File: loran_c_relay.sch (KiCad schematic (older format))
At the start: 29 parts, among them IC501 PC817, IC502 PC817, IC503 PC817, IC504 PC817, P501 RELAY A, P502 RELAY B, P503 RELAY C, P504 RELAY D, Q501 BC847, Q502 BC847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

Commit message: FIXED: no more buses on hierarchical sheet ports
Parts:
- C501: value 2.2u 6.3V -> 10u 6.3V Ta
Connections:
- net labels added: RELAY1, RELAY2, RELAY3, RELAY4
- net labels removed: BREL, REL1, REL2, REL3, REL4, RELAY
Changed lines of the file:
@@
 $Descr A4 11693 8268
 encoding utf-8
-Sheet 5 7
+Sheet 4 7
 Title ""
 Date ""
@@
 $EndComp
 $Comp
-L GND #PWR078
+L GND #PWR071
 U 1 1 52DF2D2C
 P 5500 2400
-F 0 "#PWR078" H 5500 2400 30  0001 C CNN
+F 0 "#PWR071" H 5500 2400 30  0001 C CNN
 F 1 "GND" H 5500 2330 30  0001 C CNN
 F 2 "" H 5500 2400 60  0000 C CNN
@@
 $EndComp
 $Comp
-L GND #PWR079
+L GND #PWR072
 U 1 1 52DF2D32
 P 4400 2400
-F 0 "#PWR079" H 4400 2400 30  0001 C CNN
+F 0 "#PWR072" H 4400 2400 30  0001 C CNN
 F 1 "GND" H 4400 2330 30  0001 C CNN
 F 2 "" H 4400 2400 60  0000 C CNN
@@
 $EndComp
 $Comp
-L VDD #PWR080
+L VDD #PWR073
 U 1 1 52DF2D44
 P 5150 1500
-F 0 "#PWR080" H 5150 1600 30  0001 C CNN
+F 0 "#PWR073" H 5150 1600 30  0001 C CNN
 F 1 "VDD" H 5150 1610 30  0000 C CNN
 F 2 "" H 5150 1500 60  0000 C CNN
@@
 $EndComp
 $Comp
-L GND #PWR081
+L GND #PWR074
 U 1 1 52DF2D68
 P 5500 3400
-F 0 "#PWR081" H 5500 3400 30  0001 C CNN
+F 0 "#PWR074" H 5500 3400 30  0001 C CNN
 F 1 "GND" H 5500 3330 30  0001 C CNN
 F 2 "" H 5500 3400 60  0000 C CNN
@@
 $EndComp
 $Comp
-L GND #PWR082
+L GND #PWR075
 U 1 1 52DF2D6E
 P 4400 3400
-F 0 "#PWR082" H 4400 3400 30  0001 C CNN
+F 0 "#PWR075" H 4400 3400 30  0001 C CNN
 F 1 "GND" H 4400 3330 30  0001 C CNN
 F 2 "" H 4400 3400 60  0000 C CNN
@@
 $EndComp
 $Comp
-L GND #PWR083
+L GND #PWR076
 U 1 1 52DF2D9E
 P 5500 4400
-F 0 "#PWR083" H 5500 4400 30  0001 C CNN
+F 0 "#PWR076" H 5500 4400 30  0001 C CNN
 F 1 "GND" H 5500 4330 30  0001 C CNN
 F 2 "" H 5500 4400 60  0000 C CNN
@@
 $EndComp
 $Comp
-L GND #PWR084
+L GND #PWR077
 U 1 1 52DF2DA4
 P 4400 4400
-F 0 "#PWR084" H 4400 4400 30  0001 C CNN
+F 0 "#PWR077" H 4400 4400 30  0001 C CNN
 F 1 "GND" H 4400 4330 30  0001 C CNN
 F 2 "" H 4400 4400 60  0000 C CNN
@@
 $EndComp
 $Comp
-L GND #PWR085
+L GND #PWR078
 U 1 1 52DF2DD4
 P 5500 6000
-F 0 "#PWR085" H 5500 6000 30  0001 C CNN
+F 0 "#PWR078" H 5500 6000 30  0001 C CNN
 F 1 "GND" H 5500 5930 30  0001 C CNN
 F 2 "" H 5500 6000 60  0000 C CNN
@@
 $EndComp
 $Comp
-L GND #PWR086
+L GND #PWR079
 U 1 1 52DF2DDA
 P 4400 6000
-F 0 "#PWR086" H 4400 6000 30  0001 C CNN
+F 0 "#PWR079" H 4400 6000 30  0001 C CNN
 F 1 "GND" H 4400 5930 30  0001 C CNN
 F 2 "" H 4400 6000 60  0000 C CNN
@@
 P 5150 5750
 F 0 "C501" H 5200 5850 50  0000 L CNN
-F 1 "2.2u 6.3V" H 5200 5650 50  0000 L CNN
+F 1 "10u 6.3V Ta" H 5200 5650 50  0000 L CNN
 F 2 "" H 5150 5750 60  0000 C CNN
 F 3 "" H 5150 5750 60  0000 C CNN
@@
 $EndComp
 $Comp
-L GND #PWR087
+L GND #PWR080
 U 1 1 52DF2DFE
 P 5150 6000
-F 0 "#PWR087" H 5150 6000 30  0001 C CNN
+F 0 "#PWR080" H 5150 6000 30  0001 C CNN
 F 1 "GND" H 5150 5930 30  0001 C CNN
 F 2 "" H 5150 6000 60  0000 C CNN
@@
 	1    0    0    -1
 $EndComp
-Entry Wire Line
-	4100 2050 4200 2150
-Entry Wire Line
-	4100 3050 4200 3150
-Entry Wire Line
-	4100 4050 4200 4150
-Entry Wire Line
-	4100 5050 4200 5150
-Text Label 4200 2150 0    60   ~ 0
-REL1
-Text Label 4200 3150 0    60   ~ 0
-REL2
-Text Label 4200 4150 0    60   ~ 0
-REL3
-Text Label 4200 5150 0    60   ~ 0
-REL4
-Text Label 3800 1600 0    60   ~ 0
-BREL
-Text HLabel 3800 1600 0    60   Input ~ 0
-RELAY
+Text HLabel 3800 2150 0    60   Input ~ 0
+RELAY1
+Text HLabel 3800 3150 0    60   Input ~ 0
+RELAY2
+Text HLabel 3800 4150 0    60   Input ~ 0
+RELAY3
+Text HLabel 3800 5150 0    60   Input ~ 0
+RELAY4
 Wire Wire Line
 	5500 2350 5500 2400
@@
 	5150 1500 5150 5550
 Wire Wire Line
-	4200 2150 4500 2150
+	3800 2150 4500 2150
 Wire Wire Line
 	6800 1700 6850 1700
@@
 	5150 2700 6100 2700
 Wire Wire Line
-	4200 3150 4500 3150
+	3800 3150 4500 3150
 Wire Wire Line
 	6800 2700 6850 2700
@@
 	5150 3700 6100 3700
 Wire Wire Line
-	4200 4150 4500 4150
+	3800 4150 4500 4150
 Wire Wire Line
 	6800 3700 6850 3700
@@
 	5150 4700 6100 4700
 Wire Wire Line
-	4200 5150 4500 5150
+	3800 5150 4500 5150
 Wire Wire Line
 	6800 4700 6850 4700
@@
 	5150 5950 5150 6000
 Connection ~ 5150 4700
-Wire Bus Line
-	4100 1600 4100 5050
-Wire Bus Line
-	4100 1600 3800 1600
 $EndSCHEMATC

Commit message: Update: fix, assign modules to components -Fix P302 incorrect connection -Assign footprints to components (not all yet) -Back-import footprints into schematic fields
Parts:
- removed Q501, Q502, Q503, Q504: BC847, symbol NPN
- added Q401, Q402, Q403, Q404: BC847, SMD_Packages:SOT23, symbol BC849
- C501: footprint (none) -> w_smd_capacitors:c_tant_B
- D501, D502, D503, D504: footprint (none) -> w_smd_diode:sod80c
- IC501, IC502, IC503, IC504: footprint DIP4 -> w_pth_ic:dil_4-300
- P501, P502, P503, P504: footprint (none) -> w_conn_kk100:kk100_22-23-2021
- R501, R502, R503, R504, R505, R506, R507, R508, R509, R510, R511, R512: footprint (none) -> w_smd_resistors:r_1206
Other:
- note added: "Nominal optocoupler LED current: 10mA\n\nSchottky needed to protect optocoupler\ntransistors from reverse polarity voltage"
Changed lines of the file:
@@
 encoding utf-8
 Sheet 4 7
-Title ""
+Title "Optocoupled relay drive circuit"
 Date ""
 Rev ""
-Comp ""
+Comp "Roman Dobrodiy (aka RomaVis)"
 Comment1 ""
 Comment2 ""
@@
 F 0 "R501" V 4830 2150 40  0000 C CNN
 F 1 "4.7k" V 4757 2151 40  0000 C CNN
-F 2 "" V 4680 2150 30  0000 C CNN
+F 2 "w_smd_resistors:r_1206" V 4680 2150 30  0001 C CNN
 F 3 "" H 4750 2150 30  0000 C CNN
 	1    4750 2150
@@
 F 0 "R502" V 4830 2300 40  0000 C CNN
 F 1 "10k" V 4757 2301 40  0000 C CNN
-F 2 "" V 4680 2300 30  0000 C CNN
+F 2 "w_smd_resistors:r_1206" V 4680 2300 30  0001 C CNN
 F 3 "" H 4750 2300 30  0000 C CNN
 	1    4750 2300
 	0    1    1    0
-$EndComp
-$Comp
-L NPN Q501
-U 1 1 52DF2D26
-P 5400 2150
-F 0 "Q501" H 5400 2000 50  0000 R CNN
-F 1 "BC847" H 5400 2300 50  0000 R CNN
-F 2 "" H 5400 2150 60  0000 C CNN
-F 3 "" H 5400 2150 60  0000 C CNN
-	1    5400 2150
-	1    0    0    -1
 $EndComp
 $Comp
@@
 F 0 "IC501" H 6240 1990 40  0000 C CNN
 F 1 "PC817" H 6600 1610 40  0000 C CNN
-F 2 "DIP4" H 6250 1620 30  0000 C CIN
+F 2 "w_pth_ic:dil_4-300" H 6250 1620 30  0001 C CIN
 F 3 "" H 6450 1800 60  0000 C CNN
 	1    6450 1800
@@
 F 0 "R509" V 5880 1900 40  0000 C CNN
 F 1 "200" V 5807 1901 40  0000 C CNN
-F 2 "" V 5730 1900 30  0000 C CNN
+F 2 "w_smd_resistors:r_1206" V 5730 1900 30  0001 C CNN
 F 3 "" H 5800 1900 30  0000 C CNN
 	1    5800 1900
@@
 F 0 "D501" H 7050 1900 40  0000 C CNN
 F 1 "BAS85" H 7050 1700 40  0000 C CNN
-F 2 "" H 7050 1800 60  0000 C CNN
+F 2 "w_smd_diode:sod80c" H 7050 1800 60  0001 C CNN
 F 3 "" H 7050 1800 60  0000 C CNN
 	1    7050 1800
@@
 F 0 "P501" V 7600 1800 40  0000 C CNN
 F 1 "RELAY A" V 7700 1800 40  0000 C CNN
-F 2 "" H 7650 1800 60  0000 C CNN
+F 2 "w_conn_kk100:kk100_22-23-2021" H 7650 1800 60  0001 C CNN
 F 3 "" H 7650 1800 60  0000 C CNN
 	1    7650 1800
@@
 F 0 "R503" V 4830 3150 40  0000 C CNN
 F 1 "4.7k" V 4757 3151 40  0000 C CNN
-F 2 "" V 4680 3150 30  0000 C CNN
+F 2 "w_smd_resistors:r_1206" V 4680 3150 30  0001 C CNN
 F 3 "" H 4750 3150 30  0000 C CNN
 	1    4750 3150
@@
 F 0 "R504" V 4830 3300 40  0000 C CNN
 F 1 "10k" V 4757 3301 40  0000 C CNN
-F 2 "" V 4680 3300 30  0000 C CNN
+F 2 "w_smd_resistors:r_1206" V 4680 3300 30  0001 C CNN
 F 3 "" H 4750 3300 30  0000 C CNN
 	1    4750 3300
 	0    1    1    0
-$EndComp
-$Comp
-L NPN Q502
-U 1 1 52DF2D62
-P 5400 3150
-F 0 "Q502" H 5400 3000 50  0000 R CNN
-F 1 "BC847" H 5400 3300 50  0000 R CNN
-F 2 "" H 5400 3150 60  0000 C CNN
-F 3 "" H 5400 3150 60  0000 C CNN
-	1    5400 3150
-	1    0    0    -1
 $EndComp
 $Comp
@@
 F 0 "IC502" H 6240 2990 40  0000 C CNN
 F 1 "PC817" H 6600 2610 40  0000 C CNN
-F 2 "DIP4" H 6250 2620 30  0000 C CIN
+F 2 "w_pth_ic:dil_4-300" H 6250 2620 30  0001 C CIN
 F 3 "" H 6450 2800 60  0000 C CNN
 	1    6450 2800
@@
 F 0 "R510" V 5880 2900 40  0000 C CNN
 F 1 "200" V 5807 2901 40  0000 C CNN
-F 2 "" V 5730 2900 30  0000 C CNN
+F 2 "w_smd_resistors:r_1206" V 5730 2900 30  0001 C CNN
 F 3 "" H 5800 2900 30  0000 C CNN
 	1    5800 2900
@@
 F 0 "D502" H 7050 2900 40  0000 C CNN
 F 1 "BAS85" H 7050 2700 40  0000 C CNN
-F 2 "" H 7050 2800 60  0000 C CNN
+F 2 "w_smd_diode:sod80c" H 7050 2800 60  0001 C CNN
 F 3 "" H 7050 2800 60  0000 C CNN
 	1    7050 2800
@@
 F 0 "P502" V 7600 2800 40  0000 C CNN
 F 1 "RELAY B" V 7700 2800 40  0000 C CNN
-F 2 "" H 7650 2800 60  0000 C CNN
+F 2 "w_conn_kk100:kk100_22-23-2021" H 7650 2800 60  0001 C CNN
 F 3 "" H 7650 2800 60  0000 C CNN
 	1    7650 2800
@@
 F 0 "R505" V 4830 4150 40  0000 C CNN
 F 1 "4.7k" V 4757 4151 40  0000 C CNN
-F 2 "" V 4680 4150 30  0000 C CNN
+F 2 "w_smd_resistors:r_1206" V 4680 4150 30  0001 C CNN
 F 3 "" H 4750 4150 30  0000 C CNN
 	1    4750 4150
@@
 F 0 "R506" V 4830 4300 40  0000 C CNN
 F 1 "10k" V 4757 4301 40  0000 C CNN
-F 2 "" V 4680 4300 30  0000 C CNN
+F 2 "w_smd_resistors:r_1206" V 4680 4300 30  0001 C CNN
 F 3 "" H 4750 4300 30  0000 C CNN
 	1    4750 4300
 	0    1    1    0
-$EndComp
-$Comp
-L NPN Q503
-U 1 1 52DF2D98
-P 5400 4150
-F 0 "Q503" H 5400 4000 50  0000 R CNN
-F 1 "BC847" H 5400 4300 50  0000 R CNN
-F 2 "" H 5400 4150 60  0000 C CNN
-F 3 "" H 5400 4150 60  0000 C CNN
-	1    5400 4150
-	1    0    0    -1
 $EndComp
 $Comp
@@
 F 0 "IC503" H 6240 3990 40  0000 C CNN
 F 1 "PC817" H 6600 3610 40  0000 C CNN
-F 2 "DIP4" H 6250 3620 30  0000 C CIN
+F 2 "w_pth_ic:dil_4-300" H 6250 3620 30  0001 C CIN
 F 3 "" H 6450 3800 60  0000 C CNN
 	1    6450 3800
@@
 F 0 "R511" V 5880 3900 40  0000 C CNN
 F 1 "200" V 5807 3901 40  0000 C CNN
-F 2 "" V 5730 3900 30  0000 C CNN
+F 2 "w_smd_resistors:r_1206" V 5730 3900 30  0001 C CNN
 F 3 "" H 5800 3900 30  0000 C CNN
 	1    5800 3900
@@
 F 0 "D503" H 7050 3900 40  0000 C CNN
 F 1 "BAS85" H 7050 3700 40  0000 C CNN
-F 2 "" H 7050 3800 60  0000 C CNN
+F 2 "w_smd_diode:sod80c" H 7050 3800 60  0001 C CNN
 F 3 "" H 7050 3800 60  0000 C CNN
 	1    7050 3800
@@
 F 0 "P503" V 7600 3800 40  0000 C CNN
 F 1 "RELAY C" V 7700 3800 40  0000 C CNN
-F 2 "" H 7650 3800 60  0000 C CNN
+F 2 "w_conn_kk100:kk100_22-23-2021" H 7650 3800 60  0001 C CNN
 F 3 "" H 7650 3800 60  0000 C CNN
 	1    7650 3800
@@
 F 0 "R507" V 4830 5150 40  0000 C CNN
 F 1 "4.7k" V 4757 5151 40  0000 C CNN
-F 2 "" V 4680 5150 30  0000 C CNN
+F 2 "w_smd_resistors:r_1206" V 4680 5150 30  0001 C CNN
 F 3 "" H 4750 5150 30  0000 C CNN
 	1    4750 5150
@@
 F 0 "R508" V 4830 5300 40  0000 C CNN
 F 1 "10k" V 4757 5301 40  0000 C CNN
-F 2 "" V 4680 5300 30  0000 C CNN
+F 2 "w_smd_resistors:r_1206" V 4680 5300 30  0001 C CNN
 F 3 "" H 4750 5300 30  0000 C CNN
 	1    4750 5300
 	0    1    1    0
-$EndComp
-$Comp
-L NPN Q504
-U 1 1 52DF2DCE
-P 5400 5150
-F 0 "Q504" H 5400 5000 50  0000 R CNN
-F 1 "BC847" H 5400 5300 50  0000 R CNN
-F 2 "" H 5400 5150 60  0000 C CNN
-F 3 "" H 5400 5150 60  0000 C CNN
-	1    5400 5150
-	1    0    0    -1
 $EndComp
 $Comp
@@
 F 0 "IC504" H 6240 4990 40  0000 C CNN
 F 1 "PC817" H 6600 4610 40  0000 C CNN
-F 2 "DIP4" H 6250 4620 30  0000 C CIN
+F 2 "w_pth_ic:dil_4-300" H 6250 4620 30  0001 C CIN
 F 3 "" H 6450 4800 60  0000 C CNN
 	1    6450 4800
@@
 F 0 "R512" V 5880 4900 40  0000 C CNN
 F 1 "200" V 5807 4901 40  0000 C CNN
-F 2 "" V 5730 4900 30  0000 C CNN
+F 2 "w_smd_resistors:r_1206" V 5730 4900 30  0001 C CNN
 F 3 "" H 5800 4900 30  0000 C CNN
 	1    5800 4900
@@
 F 0 "D504" H 7050 4900 40  0000 C CNN
 F 1 "BAS85" H 7050 4700 40  0000 C CNN
-F 2 "" H 7050 4800 60  0000 C CNN
+F 2 "w_smd_diode:sod80c" H 7050 4800 60  0001 C CNN
 F 3 "" H 7050 4800 60  0000 C CNN
 	1    7050 4800
@@
 F 0 "P504" V 7600 4800 40  0000 C CNN
 F 1 "RELAY D" V 7700 4800 40  0000 C CNN
-F 2 "" H 7650 4800 60  0000 C CNN
+F 2 "w_conn_kk100:kk100_22-23-2021" H 7650 4800 60  0001 C CNN
 F 3 "" H 7650 4800 60  0000 C CNN
 	1    7650 4800
@@
 F 0 "C501" H 5200 5850 50  0000 L CNN
 F 1 "10u 6.3V Ta" H 5200 5650 50  0000 L CNN
-F 2 "" H 5150 5750 60  0000 C CNN
+F 2 "w_smd_capacitors:c_tant_B" H 5150 5750 60  0001 C CNN
 F 3 "" H 5150 5750 60  0000 C CNN
 	1    5150 5750
@@
 	5150 5950 5150 6000
 Connection ~ 5150 4700
+Text Notes 5650 1300 0    60   ~ 0
+Nominal optocoupler LED current: 10mA\n\nSchottky needed to protect optocoupler\ntransistors from reverse polarity voltage
+$Comp
+L BC849 Q401
+U 1 1 52E1A755
+P 5400 2150
+F 0 "Q401" H 5400 2001 40  0000 R CNN
+F 1 "BC847" H 5400 2300 40  0000 R CNN
+F 2 "SMD_Packages:SOT23" H 5300 2252 29  0001 C CNN
+F 3 "" H 5400 2150 60  0000 C CNN
+	1    5400 2150
+	1    0    0    -1
+$EndComp
+$Comp
+L BC849 Q402
+U 1 1 52E1A773
+P 5400 3150
+F 0 "Q402" H 5400 3001 40  0000 R CNN
+F 1 "BC847" H 5400 3300 40  0000 R CNN
+F 2 "SMD_Packages:SOT23" H 5300 3252 29  0001 C CNN
+F 3 "" H 5400 3150 60  0000 C CNN
+	1    5400 3150
+	1    0    0    -1
+$EndComp
+$Comp
+L BC849 Q403
+U 1 1 52E1A77E
+P 5400 4150
+F 0 "Q403" H 5400 4001 40  0000 R CNN
+F 1 "BC847" H 5400 4300 40  0000 R CNN
+F 2 "SMD_Packages:SOT23" H 5300 4252 29  0001 C CNN
+F 3 "" H 5400 4150 60  0000 C CNN
+	1    5400 4150
+	1    0    0    -1
+$EndComp
+$Comp
+L BC849 Q404
+U 1 1 52E1A789
+P 5400 5150
+F 0 "Q404" H 5400 5001 40  0000 R CNN
+F 1 "BC847" H 5400 5300 40  0000 R CNN
+F 2 "SMD_Packages:SOT23" H 5300 5252 29  0001 C CNN
+F 3 "" H 5400 5150 60  0000 C CNN
+	1    5400 5150
+	1    0    0    -1
+$EndComp
 $EndSCHEMATC

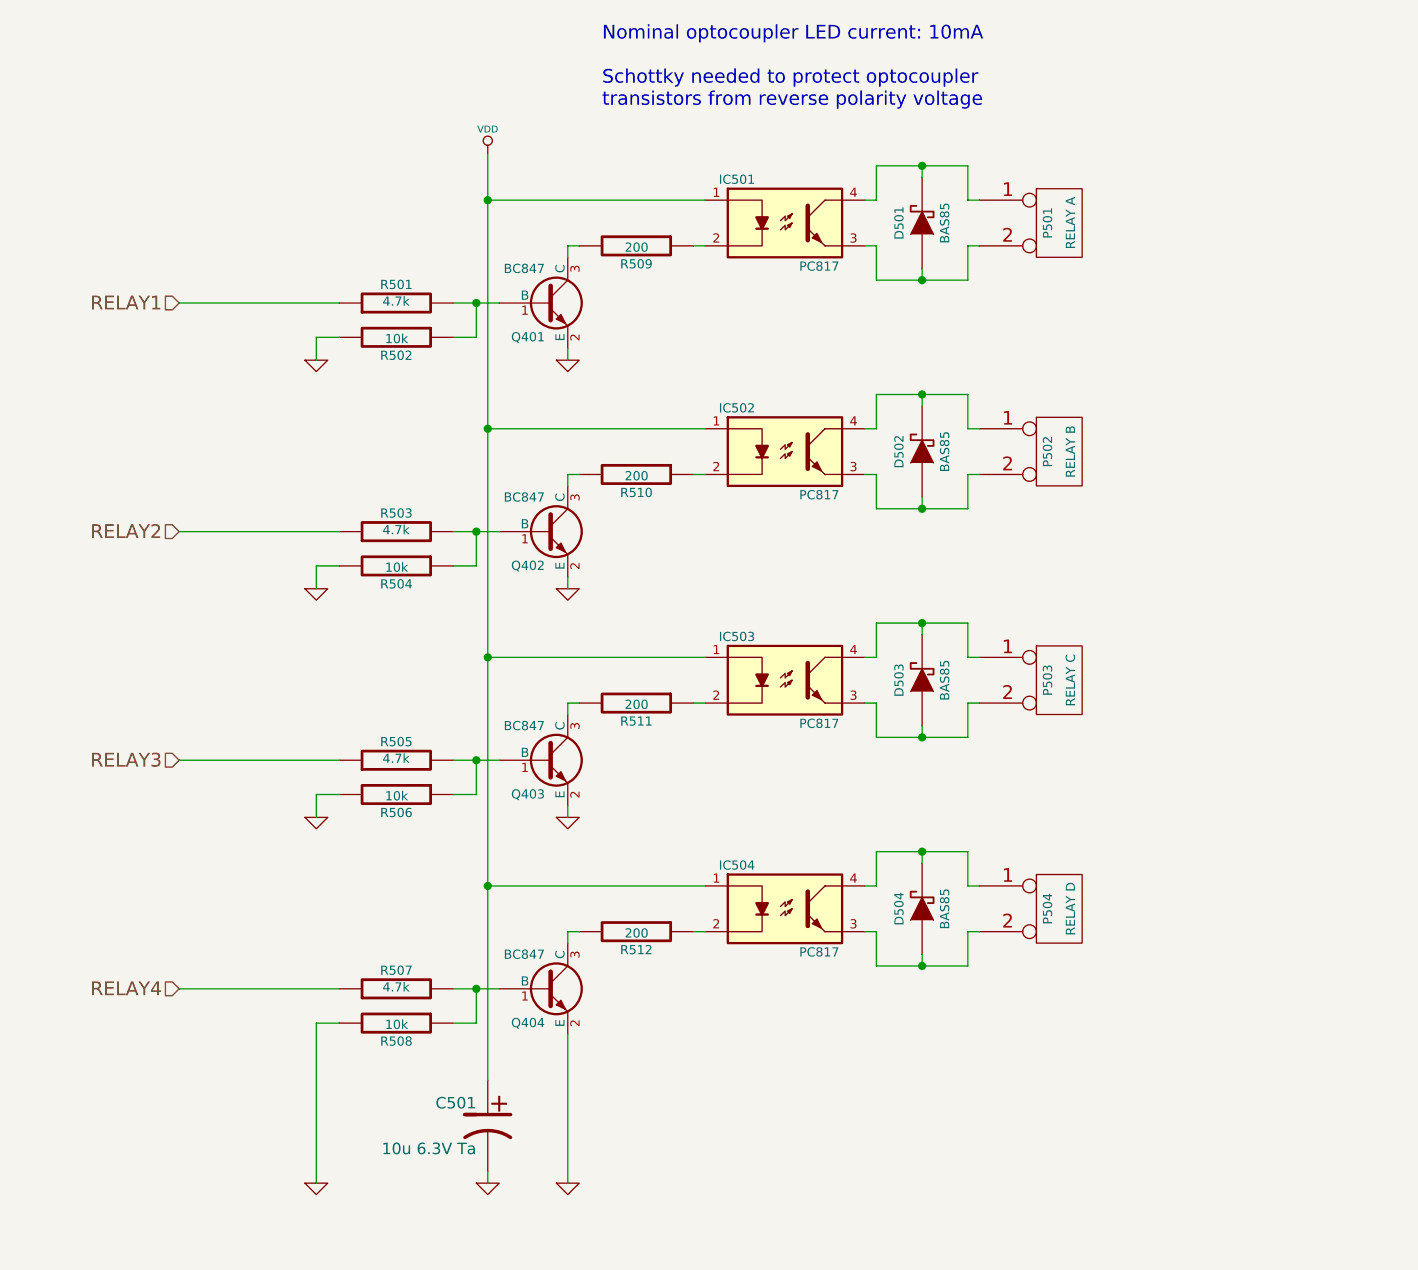
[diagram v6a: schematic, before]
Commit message: Update: lots of refactoring and pin remap ..In chase for easier PCB routing PCB still not completed
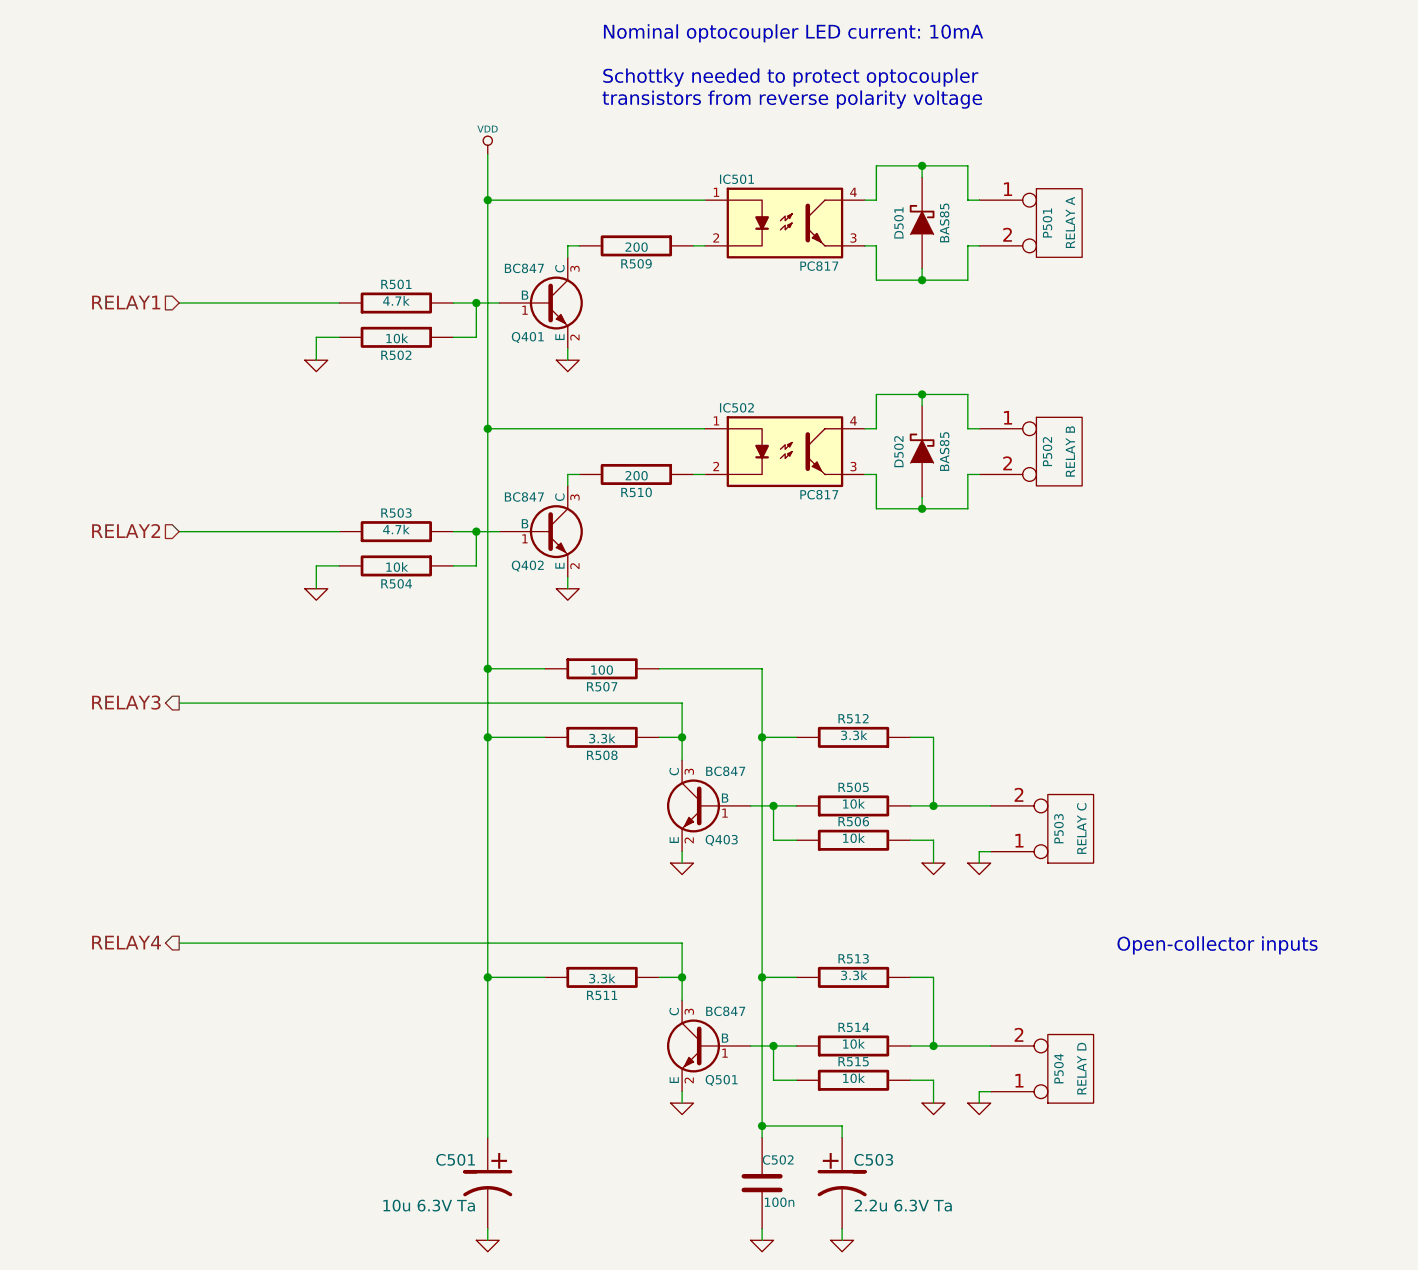
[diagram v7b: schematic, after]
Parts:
- removed D503, D504: BAS85, w_smd_diode:sod80c, symbol DIODESCH
- removed IC503, IC504: PC817, w_pth_ic:dil_4-300, symbol PC817
- removed Q404: BC847, SMD_Packages:SOT23, symbol BC849
- added C502: 100n, symbol C
- added C503: 2.2u 6.3V Ta, w_smd_capacitors:c_tant_B, symbol CP1
- added Q501: BC847, SMD_Packages:SOT23, symbol BC849
- added R513: 3.3k, w_smd_resistors:r_1206, symbol R
- added R514, R515: 10k, w_smd_resistors:r_1206, symbol R
- R505: value 4.7k -> 10k
- R507: value 4.7k -> 100
- R508: value 10k -> 3.3k
- R511, R512: value 200 -> 3.3k
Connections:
- net GND: now also P503.1 (P1), P504.1 (P1), C502.2, C503.2, Q501.2 (E), R515.2; no longer R508.2
- net RELAY3: now also Q403.3 (C), R508.2; no longer R505.1
- net RELAY4: now also R511.2, Q501.3 (C); no longer R507.1
- net VDD: now also R507.1, R508.1, R511.1
- net at Q403.1 (B), R506.1: now also R505.1; no longer R505.2
- net at P503.2 (PM): now also R505.2, R512.1
- net at R507.2: now also R512.2, C502.1, C503.1, R513.2; no longer R508.1
- net at P504.2 (PM): now also R513.1, R514.2
- new net: Q501.1 (B), R514.1, R515.1
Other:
- note added: "Open-collector inputs"
- moved on the sheet: C501, P503, P504, Q403, R505, R506
